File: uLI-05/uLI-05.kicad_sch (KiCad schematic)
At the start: 48 parts, among them J1 RJ25, J2 RJ25, J3 USB_B, J4 C, J5 PROG, Q1 IRF7306, U1 ADM2483xRW, U2 LM78M05_TO252, U3 PC817, U4 PC817, U5 PIC18F14K50-EP, Y1 12MHz

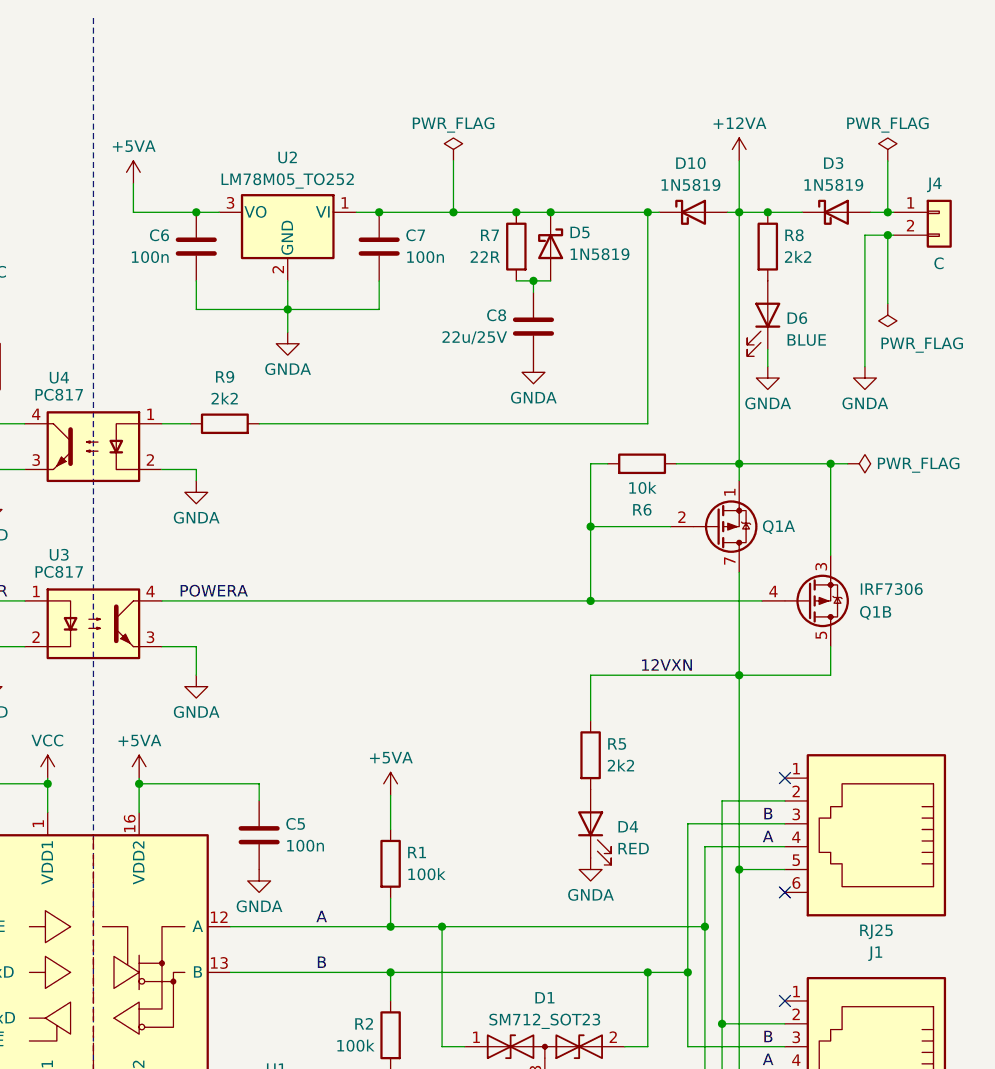
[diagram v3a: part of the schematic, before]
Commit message: Add option to bridge IRF7306 (slave variant).
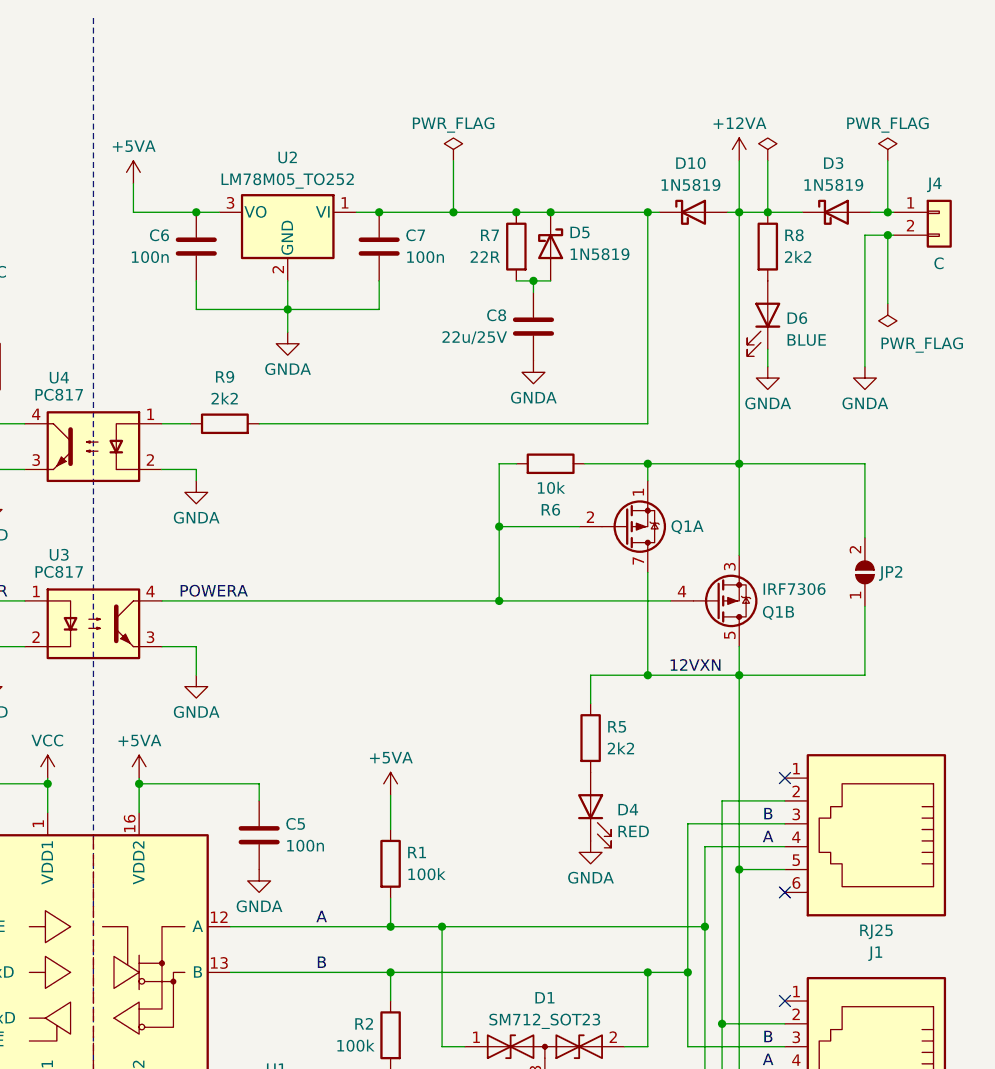
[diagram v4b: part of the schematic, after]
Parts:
- added JP2: ~, symbol Jumper:SolderJumper_2_Open
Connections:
- net +12VA: now also JP2.2 (B)
- net 12VXN: now also JP2.1 (A)
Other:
- title: uLI-05 -> uLI – Ultimate LI
- moved on the sheet: D4, Q1A, Q1B, R5, R6

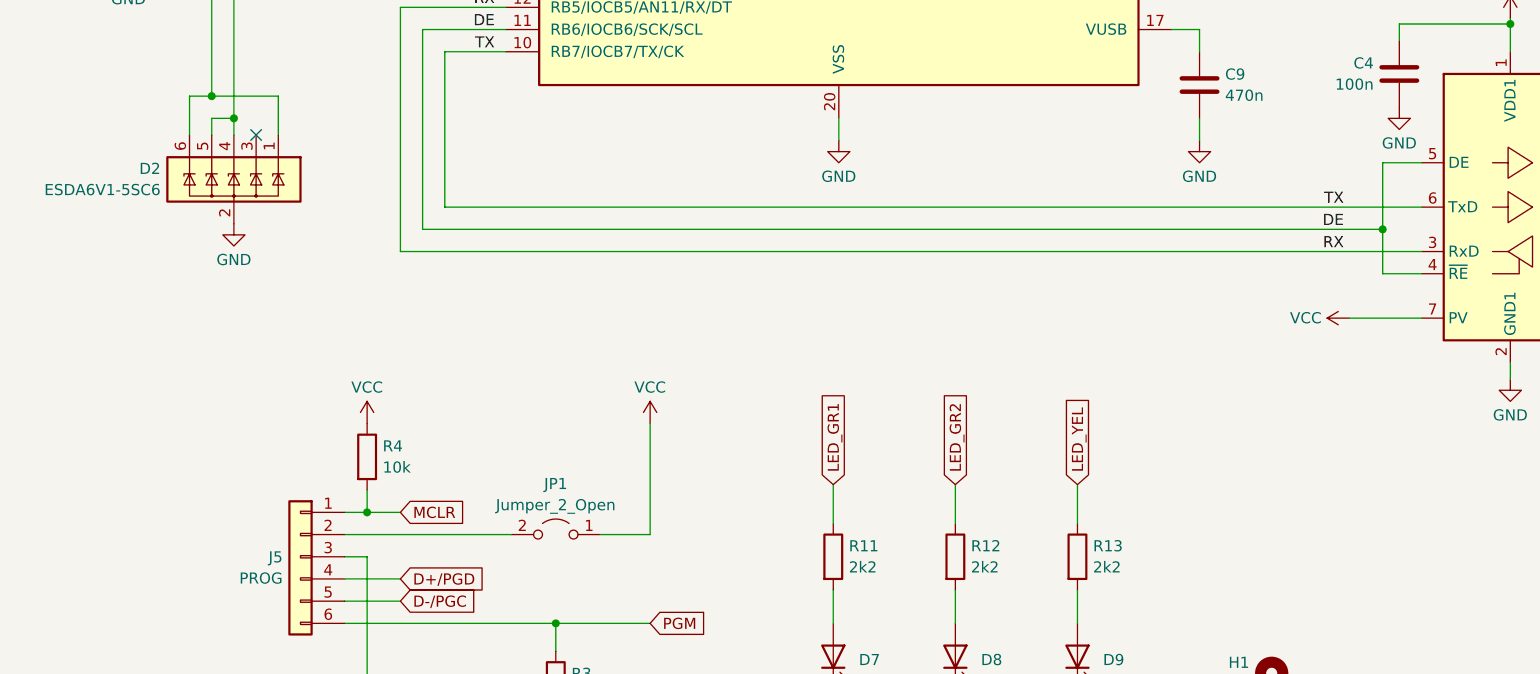
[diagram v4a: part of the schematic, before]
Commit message: Add DE pull-down.
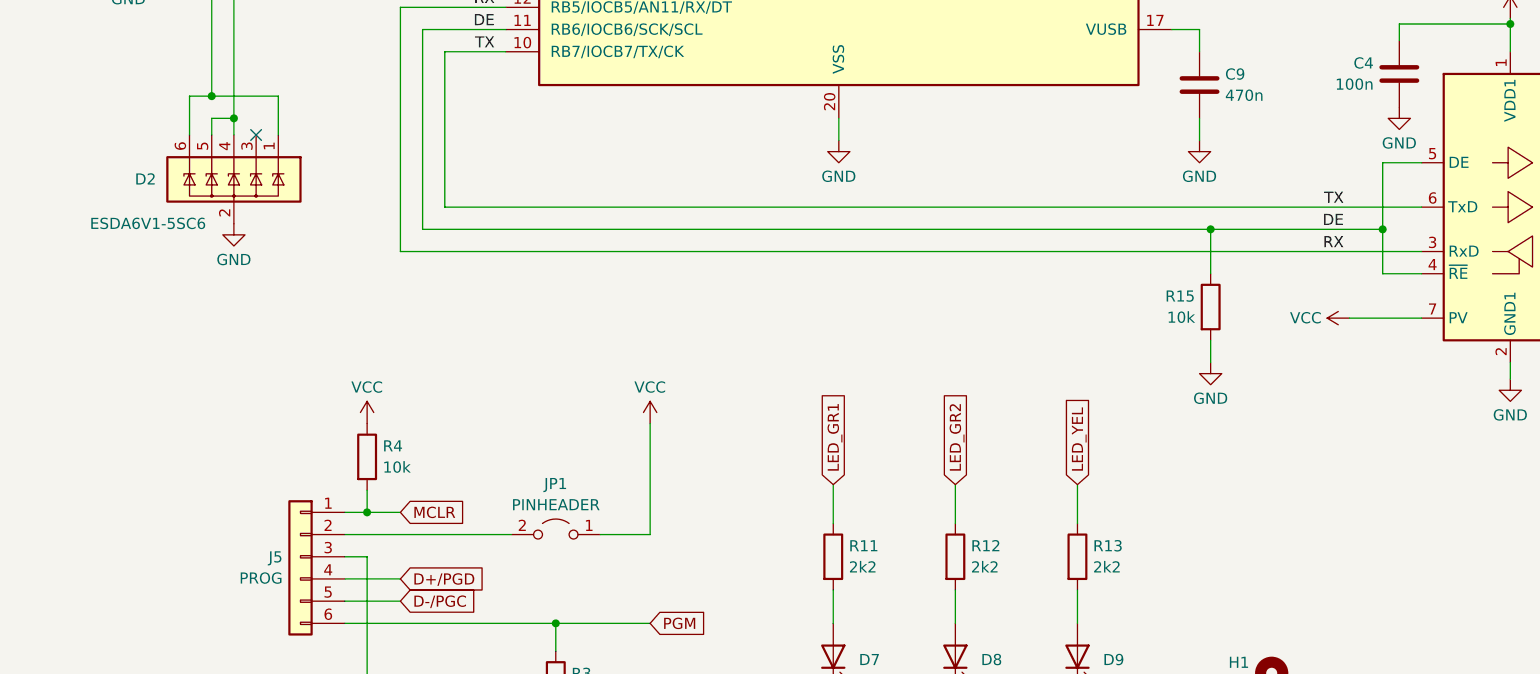
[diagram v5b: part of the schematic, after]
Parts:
- added R15: 10k, symbol Device:R
- JP1: value Jumper_2_Open -> PINHEADER
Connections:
- net DE: now also R15.1
- net GND: now also R15.2
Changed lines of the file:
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@@
   (junction (at 231.775 78.74) (diameter 0) (color 0 0 0 0)
+  )
+  (junction (at 147.32 122.555) (diameter 0) (color 0 0 0 0)
   )
   (junction (at 219.71 120.015) (diameter 0) (color 0 0 0 0)
@@
     (stroke (width 0) (type default))
   )
-  (wire (pts (xy 57.15 122.555) (xy 167.005 122.555))
+  (wire (pts (xy 57.15 122.555) (xy 147.32 122.555))
     (stroke (width 0) (type default))
   )
@@
     (stroke (width 0) (type dash))
   )
+  (wire (pts (xy 147.32 137.795) (xy 147.32 135.255))
+    (stroke (width 0) (type default))
+  )
   (wire (pts (xy 252.73 120.015) (xy 252.73 128.27))
     (stroke (width 0) (type default))
@@
     (stroke (width 0) (type default))
   )
+  (wire (pts (xy 147.32 122.555) (xy 147.32 127.635))
+    (stroke (width 0) (type default))
+  )
   (wire (pts (xy 66.675 99.695) (xy 57.15 99.695))
     (stroke (width 0) (type default))
@@
   )
   (wire (pts (xy 241.935 86.995) (xy 248.285 86.995))
+    (stroke (width 0) (type default))
+  )
+  (wire (pts (xy 147.32 122.555) (xy 167.005 122.555))
     (stroke (width 0) (type default))
   )
@@
         (path "/78ef7769-d6f1-48f5-a16b-8d45b14bfe28"
           (reference "J5") (unit 1)
+        )
+      )
+    )
+  )
+  (symbol (lib_id "power:GND") (at 147.32 137.795 0) (unit 1)
+    (in_bom yes) (on_board yes) (dnp no) (fields_autoplaced)
+    (property "Reference" "#PWR040" (at 147.32 144.145 0)
+      (effects (font (size 1.27 1.27)) hide)
+    )
+    (property "Value" "GND" (at 147.32 141.9281 0)
+      (effects (font (size 1.27 1.27)))
+    )
+    (property "Footprint" "" (at 147.32 137.795 0)
+      (effects (font (size 1.27 1.27)) hide)
+    )
+    (property "Datasheet" "" (at 147.32 137.795 0)
+      (effects (font (size 1.27 1.27)) hide)
+    )
+    (pin "1")
+    (instances
+      (project "uLI-05"
+        (path "/78ef7769-d6f1-48f5-a16b-8d45b14bfe28"
+          (reference "#PWR040") (unit 1)
         )
       )
@@
       (effects (font (size 1.27 1.27)))
     )
-    (property "Value" "Jumper_2_Open" (at 72.39 154.1089 0)
+    (property "Value" "PINHEADER" (at 72.39 154.1089 0)
       (effects (font (size 1.27 1.27)))
     )
@@
         (path "/78ef7769-d6f1-48f5-a16b-8d45b14bfe28"
           (reference "R8") (unit 1)
+        )
+      )
+    )
+  )
+  (symbol (lib_id "Device:R") (at 147.32 131.445 0) (unit 1)
+    (in_bom yes) (on_board yes) (dnp no)
+    (property "Reference" "R15" (at 145.542 130.2329 0)
+      (effects (font (size 1.27 1.27)) (justify right))
+    )
+    (property "Value" "10k" (at 145.542 132.6571 0)
+      (effects (font (size 1.27 1.27)) (justify right))
+    )
+    (property "Footprint" "" (at 145.542 131.445 90)
+      (effects (font (size 1.27 1.27)) hide)
+    )
+    (property "Datasheet" "~" (at 147.32 131.445 0)
+      (effects (font (size 1.27 1.27)) hide)
+    )
+    (pin "1")
+    (pin "2")
+    (instances
+      (project "uLI-05"
+        (path "/78ef7769-d6f1-48f5-a16b-8d45b14bfe28"
+          (reference "R15") (unit 1)
         )
       )
@@
   (symbol (lib_id "Power_Protection:ESDA6V1-5SC6") (at 35.56 116.84 0) (mirror y) (unit 1)
     (in_bom yes) (on_board yes) (dnp no)
-    (property "Reference" "D2" (at 27.178 115.6279 0)
-      (effects (font (size 1.27 1.27)) (justify left))
-    )
-    (property "Value" "ESDA6V1-5SC6" (at 27.178 118.0521 0)
-      (effects (font (size 1.27 1.27)) (justify left))
-    )
+    (property "Reference" "D2" (at 26.67 116.84 0)
+      (effects (font (size 1.27 1.27)) (justify left))
+    )
+    (property "Value" "ESDA6V1-5SC6" (at 32.385 121.92 0)
+      (effects (font (size 1.27 1.27)) (justify left))
+    )

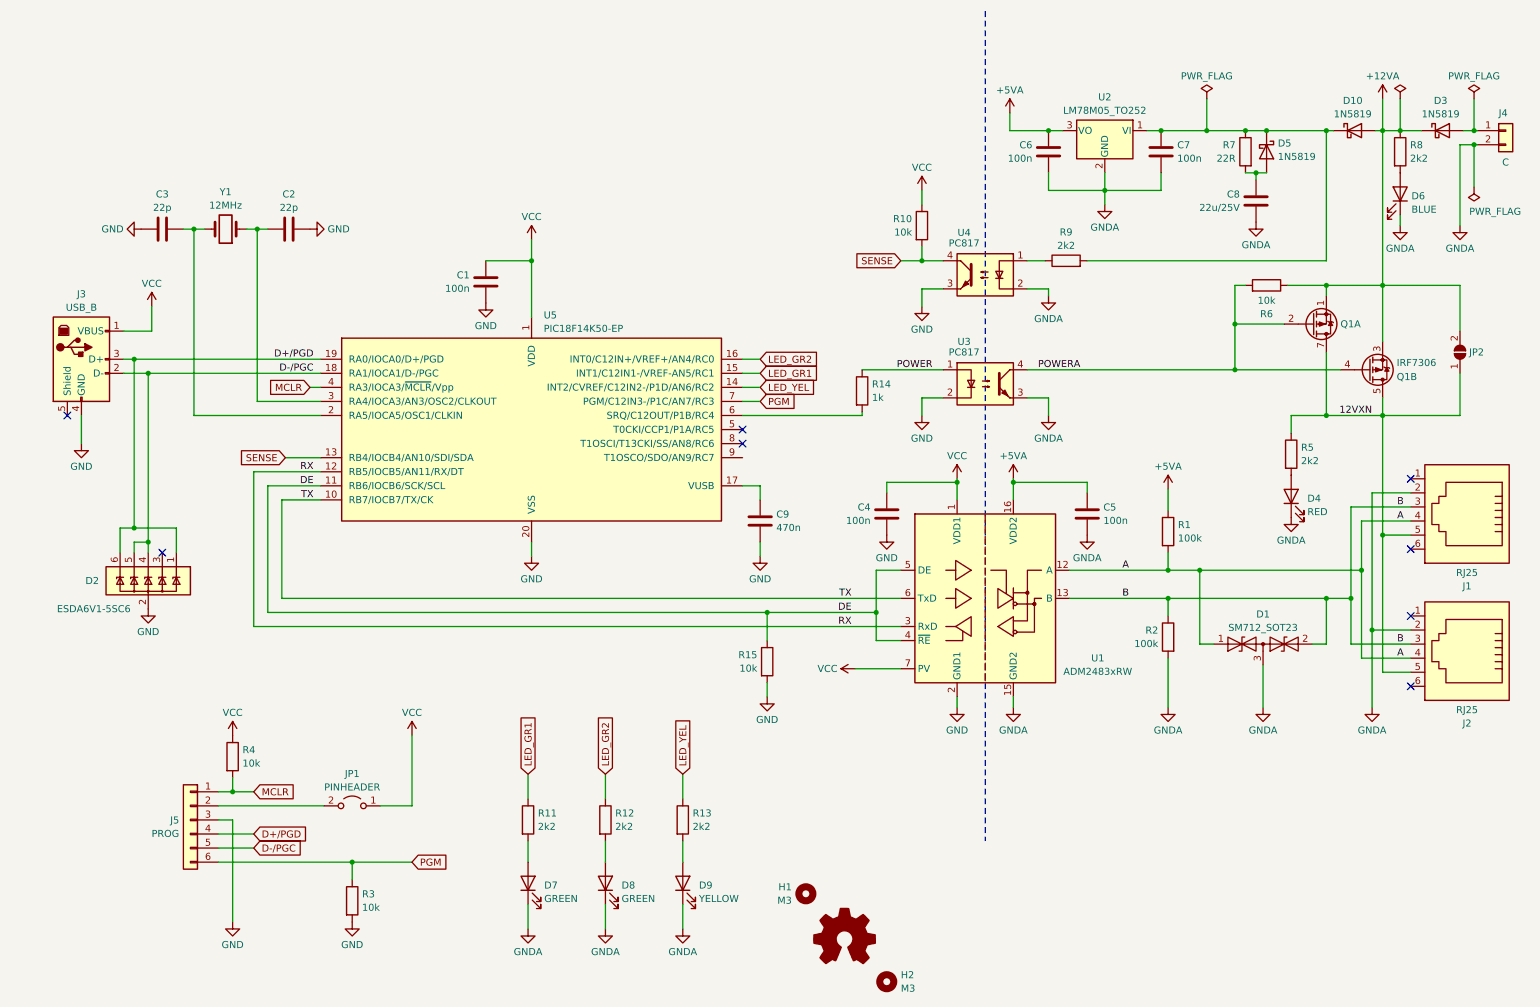
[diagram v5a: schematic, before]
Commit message: Use part names from uLI-04.
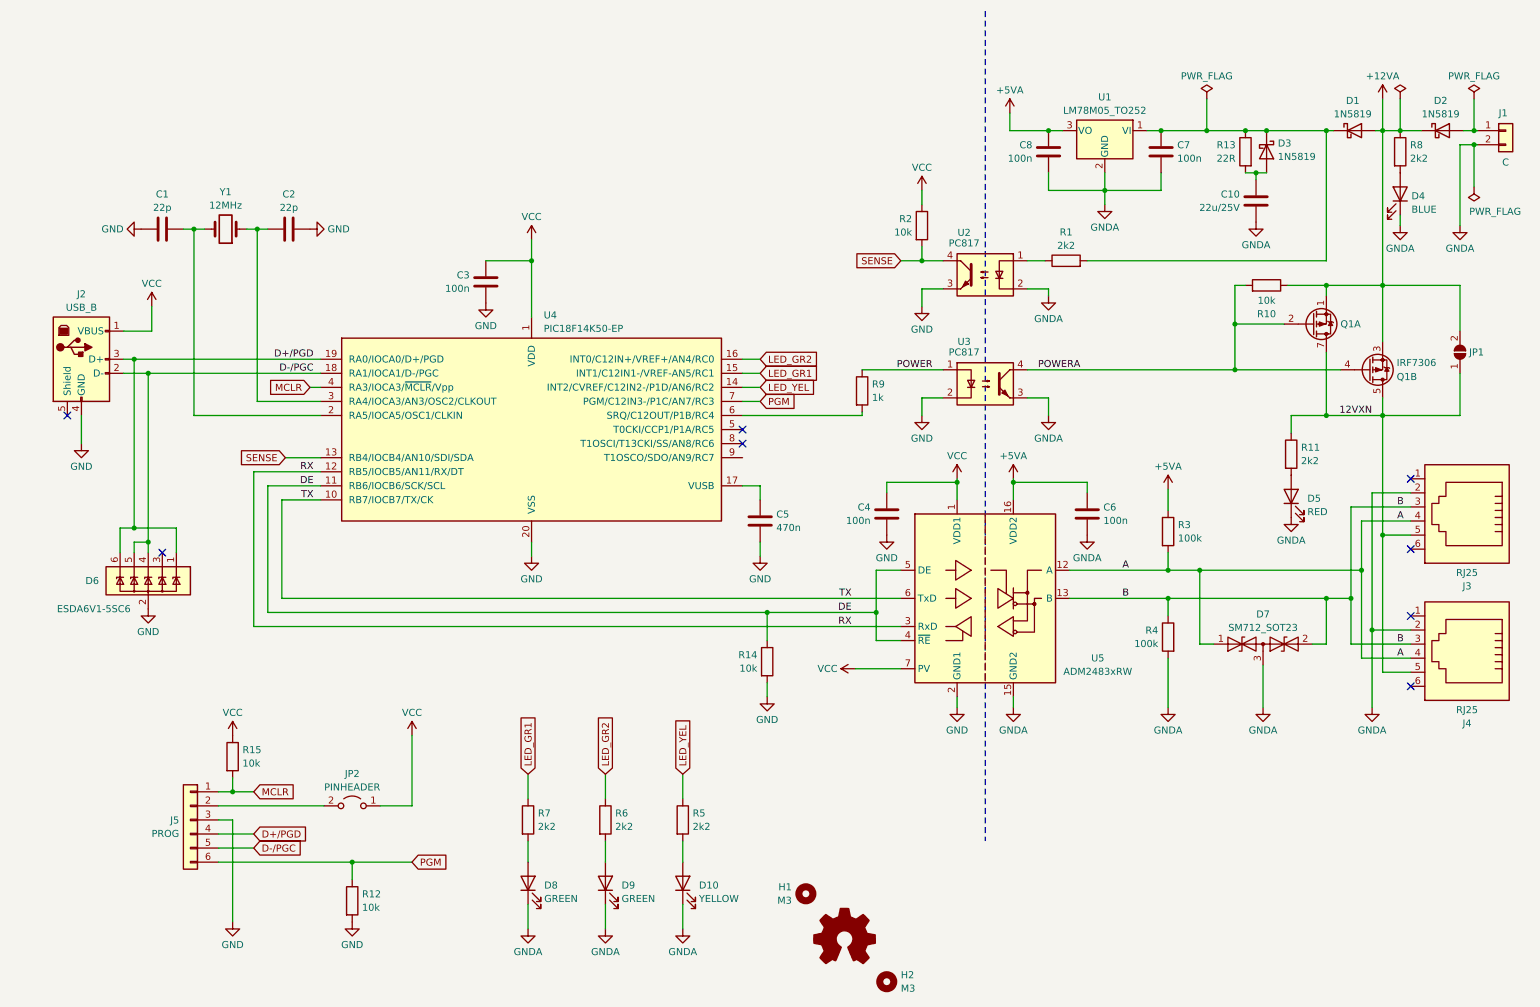
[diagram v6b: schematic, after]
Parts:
- renumbered C3 to C1, C8 to C10, C1 to C3, C9 to C5, C5 to C6, C6 to C8, D10 to D1, D9 to D10, D3 to D2, D5 to D3, D6 to D4, D4 to D5, D2 to D6, D1 to D7, D7 to D8, D8 to D9, J4 to J1, J3 to J2, J1 to J3, J2 to J4, JP2 to JP1, JP1 to JP2, R9 to R1, R6 to R10, R5 to R11, R3 to R12, R7 to R13, R15 to R14, R4 to R15, R10 to R2, R1 to R3, R2 to R4, R13 to R5, R12 to R6, R11 to R7, R14 to R9, U2 to U1, U4 to U2, U5 to U4, U1 to U5

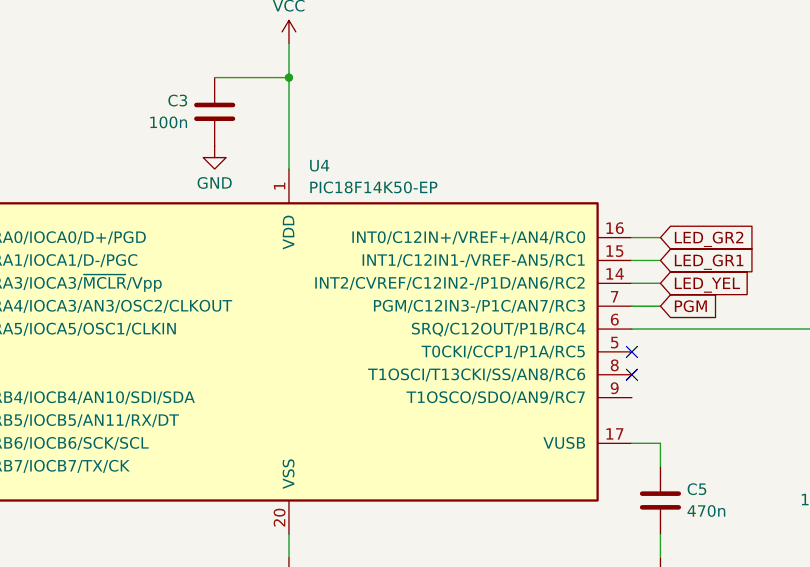
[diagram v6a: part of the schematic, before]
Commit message: Add footprints.
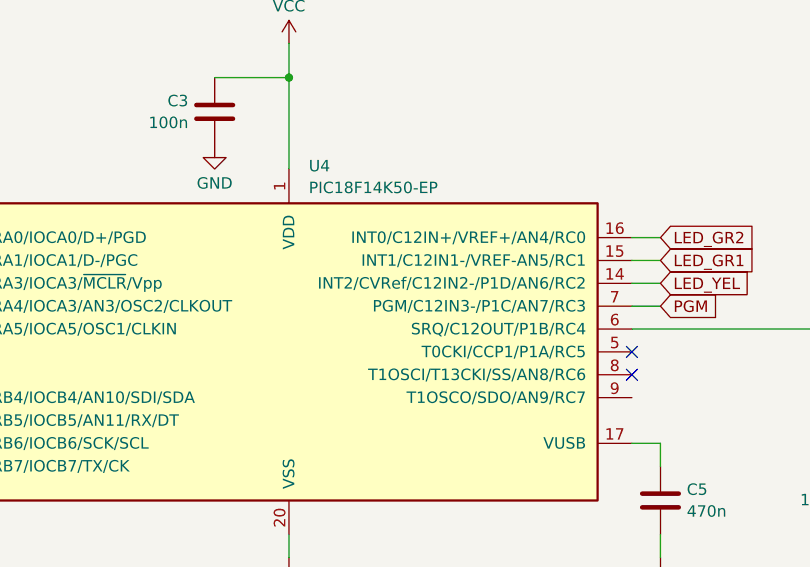
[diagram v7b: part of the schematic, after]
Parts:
- C1, C10, C2, C3, C4, C5, C6, C7, C8: footprint (none) -> Capacitor_SMD:C_0805_2012Metric
- D1, D2, D3: footprint (none) -> Diode_SMD:D_SOD-123
- D10, D4, D5, D8, D9: footprint (none) -> LED_THT:LED_D3.0mm
- H1, H2: footprint (none) -> MountingHole:MountingHole_3.2mm_M3_Pad
- J2: footprint (none) -> Connector_USB:USB_B_OST_USB-B1HSxx_Horizontal
- J3, J4: footprint (none) -> Connector_RJ:RJ12_Amphenol_54601-x06_Horizontal
- J5: footprint (none) -> Connector_PinHeader_2.54mm:PinHeader_1x06_P2.54mm_Vertical
- JP1: footprint (none) -> Jumper:SolderJumper-2_P1.3mm_Open_RoundedPad1.0x1.5mm
- JP2: footprint (none) -> Connector_PinHeader_2.54mm:PinHeader_1x02_P2.54mm_Vertical
- R1, R10, R11, R12, R13, R14, R15, R2, R3, R4, R5, R6, R7, R8, R9: footprint (none) -> Resistor_SMD:R_0805_2012Metric
- U4: footprint Package_DIP:DIP-20_W7.62mm -> Package_SO:SSOP-20_5.3x7.2mm_P0.65mm; symbol MCU_Microchip_PIC18:PIC18F14K50-EP -> MCU_Microchip_PIC18:PIC18F14K50-ESS
- Y1: footprint (none) -> Crystal:Crystal_HC49-U_Vertical
